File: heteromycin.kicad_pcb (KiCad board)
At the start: 4 copper layers, 200 x 100 mm, 379 parts, among them J1 M20-7832046, J10 DM3D-SF, J11 20021121-00010C4LF, J12 70543-0001, J13 70543-0001, J14 70543-0001, J15 70543-0001, J16 70543-0001, J17 70543-0001, J18 70543-0001, J19 70543-0001, J2 4DB-P108-06, J20 70543-0003, J21 70543-0002, J22 70543-0002, J23 70543-0002, J24 Conn_02x20_Odd_Even, J3 39531-1002, J4 39531-1002, J5 70543-0003, J6 70543-0003, J7 70543-0003, J8 70543-0003, J9 70543-0003, Q1 DMMT5401, Q10 PMPB11EN, Q11 PMPB11EN, Q12 PSMN1R2-30YLC,115, Q13 PSMN1R2-30YLC,115, Q14 PSMN1R2-30YLC,115, Q15 PMPB11EN, Q16 PMPB11EN, Q17 PMPB11EN, Q18 PMPB11EN, Q19 PMPB11EN, Q2 DMG2305UX, Q20 PMPB11EN, Q21 PMPB11EN, Q22 PMPB11EN, Q23 PMPB11EN, Q24 PMPB11EN, Q25 PMPB11EN, Q26 PMPB11EN, Q27 PMPB11EN, Q28 PMPB11EN, Q29 PMPB11EN, Q3 MMBT3904-7-F, Q30 PMPB11EN, Q31 PMPB11EN, Q32 PMPB11EN, Q33 PMPB11EN, Q34 PMPB11EN, Q35 PMPB11EN, Q36 PMPB11EN, Q37 PMPB11EN, Q38 PMPB11EN, Q39 PMPB11EN, Q4 PMPB11EN, Q40 PMPB11EN, Q41 PMPB11EN, Q42 PMPB11EN, Q43 PMPB11EN, Q44 PMPB11EN, Q45 PMPB11EN, Q46 PMPB11EN, Q47 PMPB11EN, Q48 PMPB11EN, Q49 PMPB11EN, Q5 PMPB11EN, Q50 PMPB11EN, Q6 PMPB11EN, Q7 PMPB11EN, Q8 PMPB11EN, Q9 PMPB11EN, SW1 PTS645VL39-2, U1 CAT24C32, U10 TMC2160-TA, U2 i3A, U3 AP7365-33WG-7, U4 CAT24C32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

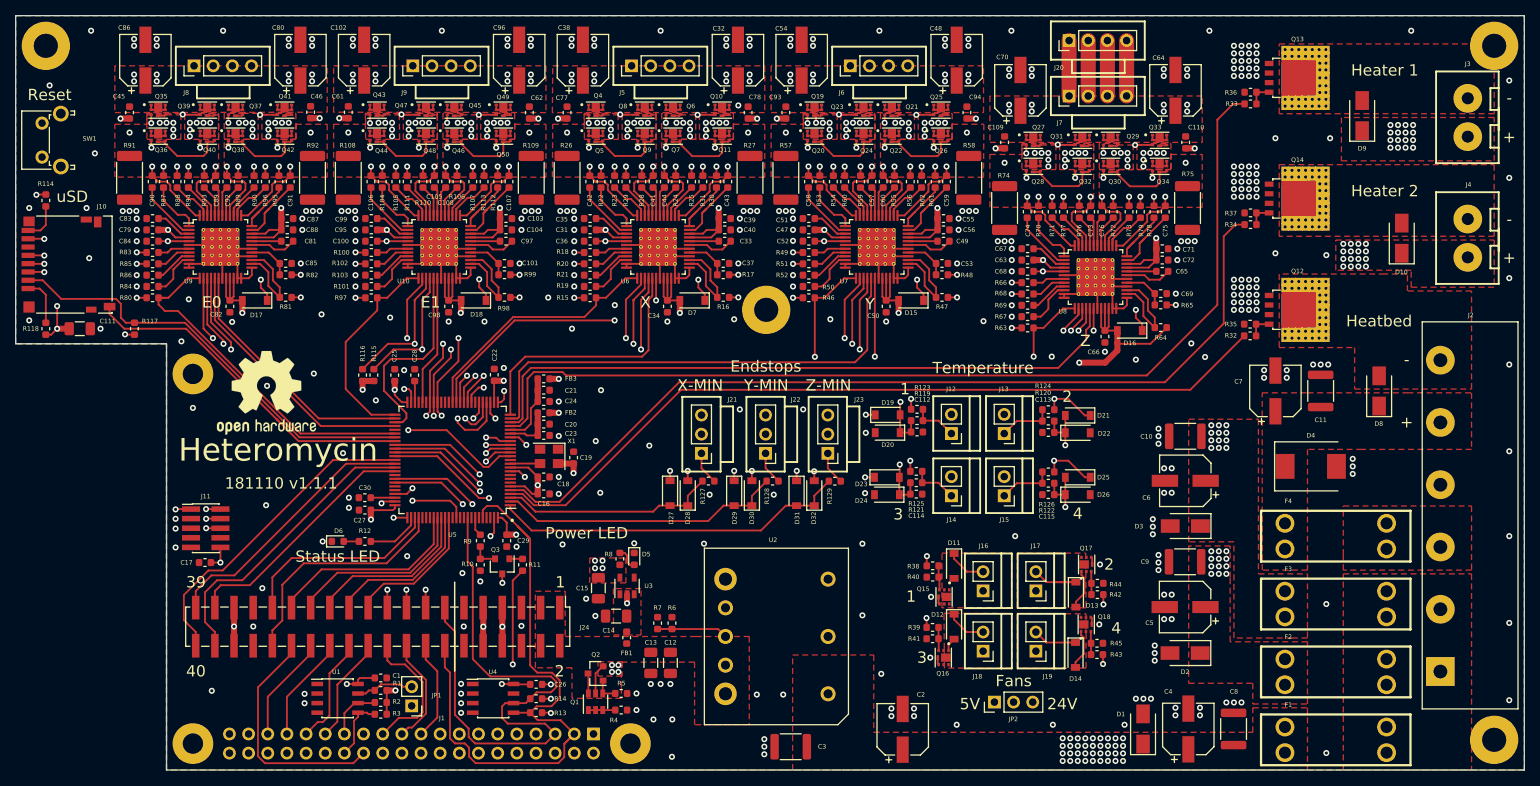
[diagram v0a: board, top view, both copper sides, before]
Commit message: Updated board to version 1.2
 * Switched small MOSFETs to SOT-23 package
 * Redesigned TMC*160 driver layout
 * Changed 01x03 to 02x03 jumper for FAN voltage selection
 * Switches STATUS_LED pin
 * Some copper pour optimizations
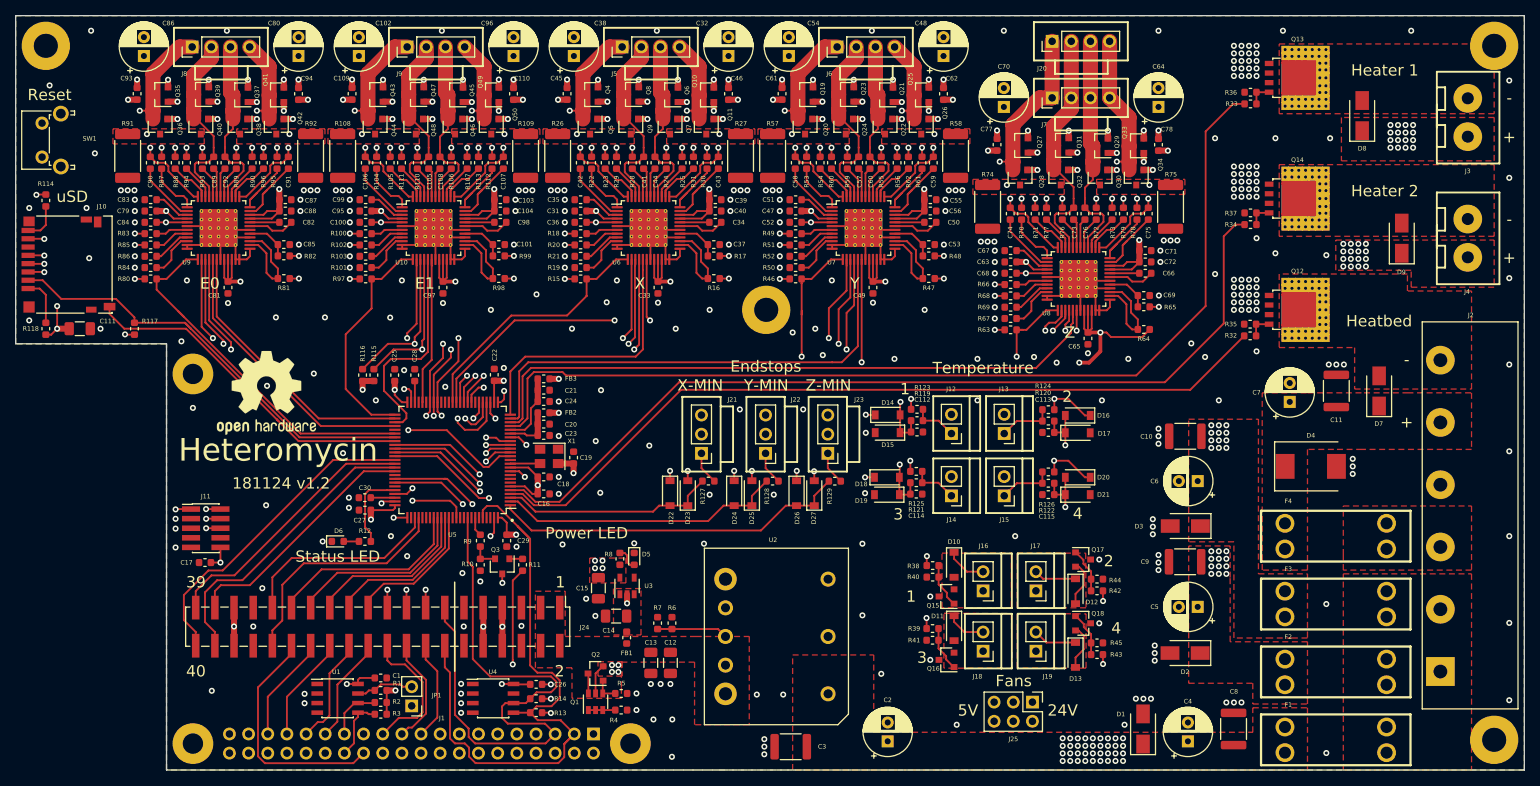
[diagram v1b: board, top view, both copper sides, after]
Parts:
- removed the D12 at (169.4, 131.0)
- removed the D15 at (163.7, 87.8)
- removed the D16 at (192.7, 91.8)
- removed the D17 at (76.7, 87.8)
- removed the D18 at (105.7, 87.8)
- removed the D7 at (134.7, 87.8)
- removed JP2: Jumper_3_Bridged12, Connector_PinHeader_2.54mm:PinHeader_1x03_P2.54mm_Vertical
- added D11: BAT54GWJ, Diode_SMD:D_SOD-123, F.Cu at (169.4, 131.2)
- added J25: Conn_02x03_Counter_Clockwise, Connector_PinHeader_2.54mm:PinHeader_2x03_P2.54mm_Vertical, F.Cu at (179.8, 141.0)
- C102, C2, C32, C38, C4, C48, C5, C54, C6, C64, C7, C70, C80, C86, C96: footprint Capacitor_SMD:CP_Elec_6.3x5.7 -> Capacitor_THT:CP_Radial_D6.3mm_P2.50mm
- C65: value 22nF -> 100nF
- C66: value 100nF -> 22nF
- Q10, Q11, Q15, Q16, Q17, Q18, Q19, Q20, Q21, Q22, Q23, Q24, Q25, Q26, Q27, Q28, Q29, Q30, Q31, Q32, Q33, Q34, Q35, Q36, Q37, Q38, Q39, Q4, Q40, Q41, Q42, Q43, Q44, Q45, Q46, Q47, Q48, Q49, Q5, Q50, Q6, Q7, Q8, Q9: value PMPB11EN -> IRLML0030TRPbF; footprint heteromycin:SOT1220 -> Package_TO_SOT_SMD:SOT-23
- moved C110 89.3 mm to (111.0, 60.4)
- moved C94 88.6 mm to (82.5, 60.4)
- moved C109 86.7 mm to (89.6, 60.4)
- moved C93 86.0 mm to (61.1, 60.4)
- moved C45 58.1 mm to (118.1, 60.4)
- moved C61 57.6 mm to (146.6, 60.4)
- moved C77 57.2 mm to (175.1, 67.1)
- moved C46 55.5 mm to (139.5, 60.4)
- moved C62 55.0 mm to (168.0, 60.4)
- moved C78 54.6 mm to (196.5, 67.1)
- moved C65 13.3 mm to (187.2, 92.8), turned to 270 degrees
- moved C66 9.95 mm to (194.8, 84.2), turned to 180 degrees
- moved Q34 3.58 mm to (193.6, 71.5), turned to 270 degrees
- moved R57 3.39 mm to (145.3, 68.6)
- moved R58 3.39 mm to (169.6, 68.6)
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- renumbered C34 to C33, C33 to C34, C50 to C49, C49 to C50, C82 to C81, C81 to C82, C98 to C97, C97 to C98, D11 to D10, D13 to D12, D14 to D13, D19 to D14, D20 to D15, D21 to D16, D22 to D17, D23 to D18, D24 to D19, D25 to D20, D26 to D21, D27 to D22, D28 to D23, D29 to D24, D30 to D25, D31 to D26, D32 to D27, D8 to D7, D9 to D8, D10 to D9
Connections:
- C65 pad 1: /Stepper Motor Z/CPO -> VDD3V3
- C65 pad 2: /Stepper Motor Z/CPI -> GND
- C66 pad 1: VDD3V3 -> /Stepper Motor Z/CPO
- C66 pad 2: GND -> /Stepper Motor Z/CPI
- J3 pad 1: VDD_HEAT1 -> HEAT1_OUT
- J3 pad 2: HEAT1_OUT -> VDD_HEAT1
- J4 pad 1: VDD_HEAT2 -> HEAT2_OUT
- J4 pad 2: HEAT2_OUT -> VDD_HEAT2
- Q10 pad 1: VDD24V -> Net-(Q10-Pad1)
- Q10 pad 3: Net-(Q10-Pad3) -> /Stepper Motor X/BMA2
- Q11 pad 1: /Stepper Motor X/BMA2 -> Net-(Q11-Pad1)
- Q15 pad 1: FAN1_OUT -> Net-(Q15-Pad1)
- Q15 pad 3: Net-(Q15-Pad3) -> GND
- Q16 pad 1: FAN3_OUT -> Net-(Q16-Pad1)
- Q16 pad 3: Net-(Q16-Pad3) -> GND
- Q17 pad 1: FAN2_OUT -> Net-(Q17-Pad1)
- Q17 pad 3: Net-(Q17-Pad3) -> GND
- Q18 pad 1: FAN4_OUT -> Net-(Q18-Pad1)
- Q18 pad 3: Net-(Q18-Pad3) -> GND
- Q19 pad 1: VDD24V -> Net-(Q19-Pad1)
- Q19 pad 3: Net-(Q19-Pad3) -> /Steper Motor Y/BMB1
- Q20 pad 1: /Steper Motor Y/BMB1 -> Net-(Q20-Pad1)
- Q21 pad 1: VDD24V -> Net-(Q21-Pad1)
- Q21 pad 3: Net-(Q21-Pad3) -> /Steper Motor Y/BMA1
- Q22 pad 1: /Steper Motor Y/BMA1 -> Net-(Q22-Pad1)
- Q23 pad 1: VDD24V -> Net-(Q23-Pad1)
- Q23 pad 3: Net-(Q23-Pad3) -> /Steper Motor Y/BMB2
- Q24 pad 1: /Steper Motor Y/BMB2 -> Net-(Q24-Pad1)
- Q24 pad 3: Net-(Q24-Pad3) -> Net-(Q20-Pad3)
- Q25 pad 1: VDD24V -> Net-(Q25-Pad1)
- Q25 pad 3: Net-(Q25-Pad3) -> /Steper Motor Y/BMA2
- Q26 pad 1: /Steper Motor Y/BMA2 -> Net-(Q26-Pad1)
- Q26 pad 3: Net-(Q26-Pad3) -> Net-(Q22-Pad3)
- Q27 pad 1: VDD24V -> Net-(Q27-Pad1)
- Q27 pad 3: Net-(Q27-Pad3) -> /Stepper Motor Z/BMB1
- Q28 pad 1: /Stepper Motor Z/BMB1 -> Net-(Q28-Pad1)
- Q29 pad 1: VDD24V -> Net-(Q29-Pad1)
- Q29 pad 3: Net-(Q29-Pad3) -> /Stepper Motor Z/BMA1
- Q30 pad 1: /Stepper Motor Z/BMA1 -> Net-(Q30-Pad1)
- Q31 pad 1: VDD24V -> Net-(Q31-Pad1)
- Q31 pad 3: Net-(Q31-Pad3) -> /Stepper Motor Z/BMB2
- Q32 pad 1: /Stepper Motor Z/BMB2 -> Net-(Q32-Pad1)
- Q32 pad 3: Net-(Q32-Pad3) -> Net-(Q28-Pad3)
- Q33 pad 1: VDD24V -> Net-(Q33-Pad1)
- Q33 pad 3: Net-(Q33-Pad3) -> /Stepper Motor Z/BMA2
- Q34 pad 1: /Stepper Motor Z/BMA2 -> Net-(Q34-Pad1)
- Q34 pad 3: Net-(Q34-Pad3) -> Net-(Q30-Pad3)
- Q35 pad 1: VDD24V -> Net-(Q35-Pad1)
- Q35 pad 3: Net-(Q35-Pad3) -> /Stepper Motor E0/BMB1
- Q36 pad 1: /Stepper Motor E0/BMB1 -> Net-(Q36-Pad1)
- Q37 pad 1: VDD24V -> Net-(Q37-Pad1)
- Q37 pad 3: Net-(Q37-Pad3) -> /Stepper Motor E0/BMA1
- Q38 pad 1: /Stepper Motor E0/BMA1 -> Net-(Q38-Pad1)
- Q39 pad 1: VDD24V -> Net-(Q39-Pad1)
- Q39 pad 3: Net-(Q39-Pad3) -> /Stepper Motor E0/BMB2
- Q4 pad 1: VDD24V -> Net-(Q4-Pad1)
- Q4 pad 3: Net-(Q4-Pad3) -> /Stepper Motor X/BMB1
- Q40 pad 1: /Stepper Motor E0/BMB2 -> Net-(Q40-Pad1)
- Q40 pad 3: Net-(Q40-Pad3) -> Net-(Q36-Pad3)
- Q41 pad 1: VDD24V -> Net-(Q41-Pad1)
- Q41 pad 3: Net-(Q41-Pad3) -> /Stepper Motor E0/BMA2
- Q42 pad 1: /Stepper Motor E0/BMA2 -> Net-(Q42-Pad1)
- Q42 pad 3: Net-(Q42-Pad3) -> Net-(Q38-Pad3)
- Q43 pad 1: VDD24V -> Net-(Q43-Pad1)
- Q43 pad 3: Net-(Q43-Pad3) -> /Stepper Motor E1/BMB1
- Q44 pad 1: /Stepper Motor E1/BMB1 -> Net-(Q44-Pad1)
- Q45 pad 1: VDD24V -> Net-(Q45-Pad1)
- Q45 pad 3: Net-(Q45-Pad3) -> /Stepper Motor E1/BMA1
- Q46 pad 1: /Stepper Motor E1/BMA1 -> Net-(Q46-Pad1)
- Q47 pad 1: VDD24V -> Net-(Q47-Pad1)
- Q47 pad 3: Net-(Q47-Pad3) -> /Stepper Motor E1/BMB2
- Q48 pad 1: /Stepper Motor E1/BMB2 -> Net-(Q48-Pad1)
- Q48 pad 3: Net-(Q48-Pad3) -> Net-(Q44-Pad3)
- Q49 pad 1: VDD24V -> Net-(Q49-Pad1)
- Q49 pad 3: Net-(Q49-Pad3) -> /Stepper Motor E1/BMA2
- Q5 pad 1: /Stepper Motor X/BMB1 -> Net-(Q5-Pad1)
- Q50 pad 1: /Stepper Motor E1/BMA2 -> Net-(Q50-Pad1)
- Q50 pad 3: Net-(Q50-Pad3) -> Net-(Q46-Pad3)
- Q6 pad 1: VDD24V -> Net-(Q6-Pad1)
- Q6 pad 3: Net-(Q6-Pad3) -> /Stepper Motor X/BMA1
- Q7 pad 1: /Stepper Motor X/BMA1 -> Net-(Q7-Pad1)
- Q7 pad 3: Net-(Q7-Pad3) -> Net-(Q11-Pad3)
- Q8 pad 1: VDD24V -> Net-(Q8-Pad1)
- Q8 pad 3: Net-(Q8-Pad3) -> /Stepper Motor X/BMB2
- Q9 pad 1: /Stepper Motor X/BMB2 -> Net-(Q9-Pad1)
- Q9 pad 3: Net-(Q9-Pad3) -> Net-(Q5-Pad3)
- R100 pad 1: Net-(Q44-Pad4) -> Net-(Q44-Pad3)
- R102 pad 2: Net-(Q46-Pad4) -> Net-(Q46-Pad3)
- R104 pad 2: Net-(Q43-Pad3) -> Net-(Q43-Pad1)
- R105 pad 2: Net-(Q44-Pad3) -> Net-(Q44-Pad1)
- R106 pad 2: Net-(Q45-Pad3) -> Net-(Q45-Pad1)
- R107 pad 2: Net-(Q46-Pad3) -> Net-(Q46-Pad1)
- R108 pad 2: Net-(Q44-Pad4) -> Net-(Q44-Pad3)
- R109 pad 2: Net-(Q46-Pad4) -> Net-(Q46-Pad3)
- R110 pad 1: Net-(Q47-Pad3) -> Net-(Q47-Pad1)
- R111 pad 1: Net-(Q48-Pad3) -> Net-(Q48-Pad1)
- R112 pad 1: Net-(Q49-Pad3) -> Net-(Q49-Pad1)
- R113 pad 1: Net-(Q50-Pad3) -> Net-(Q50-Pad1)
- R18 pad 1: Net-(Q5-Pad4) -> Net-(Q5-Pad3)
- R20 pad 2: Net-(Q11-Pad4) -> Net-(Q11-Pad3)
- R22 pad 2: Net-(Q4-Pad3) -> Net-(Q4-Pad1)
- R23 pad 2: Net-(Q5-Pad3) -> Net-(Q5-Pad1)
- R24 pad 2: Net-(Q6-Pad3) -> Net-(Q6-Pad1)
- R25 pad 2: Net-(Q7-Pad3) -> Net-(Q7-Pad1)
- R26 pad 2: Net-(Q5-Pad4) -> Net-(Q5-Pad3)
- R27 pad 2: Net-(Q11-Pad4) -> Net-(Q11-Pad3)
- R28 pad 1: Net-(Q8-Pad3) -> Net-(Q8-Pad1)
- R29 pad 1: Net-(Q9-Pad3) -> Net-(Q9-Pad1)
- R30 pad 1: Net-(Q10-Pad3) -> Net-(Q10-Pad1)
- R31 pad 1: Net-(Q11-Pad3) -> Net-(Q11-Pad1)
- R38 pad 1: Net-(Q15-Pad3) -> Net-(Q15-Pad1)
- R39 pad 1: Net-(Q16-Pad3) -> Net-(Q16-Pad1)
- R40 pad 2: Net-(Q15-Pad3) -> Net-(Q15-Pad1)
- R41 pad 2: Net-(Q16-Pad3) -> Net-(Q16-Pad1)
- R42 pad 1: Net-(Q17-Pad3) -> Net-(Q17-Pad1)
- R43 pad 1: Net-(Q18-Pad3) -> Net-(Q18-Pad1)
- R44 pad 2: Net-(Q17-Pad3) -> Net-(Q17-Pad1)
- R45 pad 2: Net-(Q18-Pad3) -> Net-(Q18-Pad1)
- R49 pad 1: Net-(Q20-Pad4) -> Net-(Q20-Pad3)
- R51 pad 2: Net-(Q22-Pad4) -> Net-(Q22-Pad3)
- R53 pad 2: Net-(Q19-Pad3) -> Net-(Q19-Pad1)
- R54 pad 2: Net-(Q20-Pad3) -> Net-(Q20-Pad1)
- R55 pad 2: Net-(Q21-Pad3) -> Net-(Q21-Pad1)
- R56 pad 2: Net-(Q22-Pad3) -> Net-(Q22-Pad1)
- R57 pad 2: Net-(Q20-Pad4) -> Net-(Q20-Pad3)
- R58 pad 2: Net-(Q22-Pad4) -> Net-(Q22-Pad3)
- R59 pad 1: Net-(Q23-Pad3) -> Net-(Q23-Pad1)
- R60 pad 1: Net-(Q24-Pad3) -> Net-(Q24-Pad1)
- R61 pad 1: Net-(Q25-Pad3) -> Net-(Q25-Pad1)
- R62 pad 1: Net-(Q26-Pad3) -> Net-(Q26-Pad1)
- R66 pad 1: Net-(Q28-Pad4) -> Net-(Q28-Pad3)
- R68 pad 2: Net-(Q30-Pad4) -> Net-(Q30-Pad3)
- R70 pad 2: Net-(Q27-Pad3) -> Net-(Q27-Pad1)
- R71 pad 2: Net-(Q28-Pad3) -> Net-(Q28-Pad1)
- R72 pad 2: Net-(Q29-Pad3) -> Net-(Q29-Pad1)
- R73 pad 2: Net-(Q30-Pad3) -> Net-(Q30-Pad1)
- R74 pad 2: Net-(Q28-Pad4) -> Net-(Q28-Pad3)
- R75 pad 2: Net-(Q30-Pad4) -> Net-(Q30-Pad3)
- R76 pad 1: Net-(Q31-Pad3) -> Net-(Q31-Pad1)
- R77 pad 1: Net-(Q32-Pad3) -> Net-(Q32-Pad1)
- R78 pad 1: Net-(Q33-Pad3) -> Net-(Q33-Pad1)
- R79 pad 1: Net-(Q34-Pad3) -> Net-(Q34-Pad1)
- R83 pad 1: Net-(Q36-Pad4) -> Net-(Q36-Pad3)
- R85 pad 2: Net-(Q38-Pad4) -> Net-(Q38-Pad3)
- R87 pad 2: Net-(Q35-Pad3) -> Net-(Q35-Pad1)
- R88 pad 2: Net-(Q36-Pad3) -> Net-(Q36-Pad1)
- R89 pad 2: Net-(Q37-Pad3) -> Net-(Q37-Pad1)
- R90 pad 2: Net-(Q38-Pad3) -> Net-(Q38-Pad1)
- R91 pad 2: Net-(Q36-Pad4) -> Net-(Q36-Pad3)
- R92 pad 2: Net-(Q38-Pad4) -> Net-(Q38-Pad3)
- R93 pad 1: Net-(Q39-Pad3) -> Net-(Q39-Pad1)
- R94 pad 1: Net-(Q40-Pad3) -> Net-(Q40-Pad1)
- R95 pad 1: Net-(Q41-Pad3) -> Net-(Q41-Pad1)
- R96 pad 1: Net-(Q42-Pad3) -> Net-(Q42-Pad1)
- U5 pad 71: Net-(U5-Pad71) -> /MCU/STATUS_LED
- U5 pad 77: /MCU/STATUS_LED -> Net-(U5-Pad77)
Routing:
- net VDD24V: track 162.7 -> 110.5 mm, vias 92 -> 76
- net Net-(Q28-Pad4): track 47.2 -> 0.00 mm, vias 2 -> 0
- net Net-(Q20-Pad4): track 47.2 -> 0.00 mm, vias 2 -> 0
- net Net-(Q5-Pad4): track 47.2 -> 0.00 mm, vias 2 -> 0
- net Net-(Q44-Pad4): track 47.2 -> 0.00 mm, vias 2 -> 0
- net Net-(Q36-Pad4): track 47.2 -> 0.00 mm, vias 2 -> 0
- net Net-(Q11-Pad4): track 44.4 -> 0.00 mm, vias 2 -> 0
- net Net-(Q30-Pad4): track 44.4 -> 0.00 mm, vias 2 -> 0
- net Net-(Q22-Pad4): track 44.4 -> 0.00 mm, vias 2 -> 0
- net Net-(Q46-Pad4): track 44.4 -> 0.00 mm, vias 2 -> 0
- net Net-(Q38-Pad4): track 44.4 -> 0.00 mm, vias 2 -> 0
- net Net-(Q11-Pad3): track 5.30 -> 31.6 mm
- net Net-(Q36-Pad3): track 6.58 -> 31.7 mm
- net Net-(Q5-Pad3): track 6.58 -> 31.7 mm
- net Net-(Q44-Pad3): track 6.58 -> 31.7 mm
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- added copper zone on F.Cu, net Net-(Q11-Pad3)
- added copper zone on F.Cu, net Net-(Q20-Pad3)
- added copper zone on F.Cu, net Net-(Q22-Pad3)
- added copper zone on F.Cu, net Net-(Q28-Pad3)
- added copper zone on F.Cu, net Net-(Q30-Pad3)
- added copper zone on F.Cu, net Net-(Q36-Pad3)
- added copper zone on F.Cu, net Net-(Q38-Pad3)
- added copper zone on F.Cu, net Net-(Q44-Pad3)
- added copper zone on F.Cu, net Net-(Q46-Pad3)
- added copper zone on F.Cu, net Net-(Q5-Pad3)
- removed copper zone on F.Cu, net /Steper Motor Y/BMA1
- removed copper zone on In2.Cu, net /Steper Motor Y/BMA1
- removed copper zone on F.Cu, net /Steper Motor Y/BMA2
- removed copper zone on In2.Cu, net /Steper Motor Y/BMA2
- removed copper zone on F.Cu, net /Steper Motor Y/BMB1
- removed copper zone on In2.Cu, net /Steper Motor Y/BMB1
- removed copper zone on F.Cu, net /Steper Motor Y/BMB2
- removed copper zone on In2.Cu, net /Steper Motor Y/BMB2
- removed copper zone on F.Cu, net /Stepper Motor E0/BMA1
- removed copper zone on In2.Cu, net /Stepper Motor E0/BMA1
- removed copper zone on F.Cu, net /Stepper Motor E0/BMA2
- removed copper zone on In2.Cu, net /Stepper Motor E0/BMA2
- removed copper zone on F.Cu, net /Stepper Motor E0/BMB1
- removed copper zone on In2.Cu, net /Stepper Motor E0/BMB1
- removed copper zone on F.Cu, net /Stepper Motor E0/BMB2
- removed copper zone on In2.Cu, net /Stepper Motor E0/BMB2
- removed copper zone on F.Cu, net /Stepper Motor E1/BMA1
- removed copper zone on In2.Cu, net /Stepper Motor E1/BMA1
- removed copper zone on F.Cu, net /Stepper Motor E1/BMA2
- removed copper zone on In2.Cu, net /Stepper Motor E1/BMA2
- removed copper zone on F.Cu, net /Stepper Motor E1/BMB1
- removed copper zone on In2.Cu, net /Stepper Motor E1/BMB1
- removed copper zone on F.Cu, net /Stepper Motor E1/BMB2
- removed copper zone on In2.Cu, net /Stepper Motor E1/BMB2
- removed copper zone on F.Cu, net /Stepper Motor X/BMA1
- removed copper zone on In2.Cu, net /Stepper Motor X/BMA1
- removed copper zone on F.Cu, net /Stepper Motor X/BMA2
- removed copper zone on In2.Cu, net /Stepper Motor X/BMA2
- removed copper zone on F.Cu, net /Stepper Motor X/BMB1
- removed copper zone on In2.Cu, net /Stepper Motor X/BMB1
- removed copper zone on F.Cu, net /Stepper Motor X/BMB2
- removed copper zone on In2.Cu, net /Stepper Motor X/BMB2
- removed copper zone on F.Cu, net /Stepper Motor Z/BMA1
- removed copper zone on In2.Cu, net /Stepper Motor Z/BMA1
- removed copper zone on F.Cu, net /Stepper Motor Z/BMA2
- removed copper zone on In2.Cu, net /Stepper Motor Z/BMA2
- removed copper zone on F.Cu, net /Stepper Motor Z/BMB1
- removed copper zone on In2.Cu, net /Stepper Motor Z/BMB1
- removed copper zone on F.Cu, net /Stepper Motor Z/BMB2
- removed copper zone on In2.Cu, net /Stepper Motor Z/BMB2
- removed copper zone on F.Cu, net Net-(Q11-Pad4)
- removed copper zone on F.Cu, net Net-(Q20-Pad4)
- removed copper zone on F.Cu, net Net-(Q22-Pad4)
- removed copper zone on F.Cu, net Net-(Q28-Pad4)
- removed copper zone on F.Cu, net Net-(Q30-Pad4)
- removed copper zone on F.Cu, net Net-(Q36-Pad4)
- removed copper zone on F.Cu, net Net-(Q38-Pad4)
- removed copper zone on F.Cu, net Net-(Q44-Pad4)
- removed copper zone on F.Cu, net Net-(Q46-Pad4)
- removed copper zone on F.Cu, net Net-(Q5-Pad4)
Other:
- board text added: "181124 v1.2"
- board text removed: "181110 v1.1.1"

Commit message: Increased sense resistor value to 0.1
This will result in a maximum 2.3A current for the stepper.
This should act as a more sensible default. Of course the user
can replace the sense resistors as they see fit. As long as they
they don't stress the termal budget of the driver MOSFET that is.
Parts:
- R108, R109, R26, R27, R57, R58, R74, R75, R91, R92: value 0.075 -> 0.1
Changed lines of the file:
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@@
       (effects (font (size 0.6 0.6) (thickness 0.1)))
     )
-    (fp_text value 0.075 (at 0 2.62 90) (layer F.Fab)
+    (fp_text value 0.1 (at 0 2.62 90) (layer F.Fab)
       (effects (font (size 0.6 0.6) (thickness 0.1)))
     )
@@
       (effects (font (size 0.6 0.6) (thickness 0.1)))
     )
-    (fp_text value 0.075 (at 0 2.62 90) (layer F.Fab)
+    (fp_text value 0.1 (at 0 2.62 90) (layer F.Fab)
       (effects (font (size 0.6 0.6) (thickness 0.1)))
     )
@@
       (effects (font (size 0.6 0.6) (thickness 0.1)))
     )
-    (fp_text value 0.075 (at 0 2.62 90) (layer F.Fab)
+    (fp_text value 0.1 (at 0 2.62 90) (layer F.Fab)
       (effects (font (size 0.6 0.6) (thickness 0.1)))
     )
@@
       (effects (font (size 0.6 0.6) (thickness 0.1)))
     )
-    (fp_text value 0.075 (at 0 2.62 90) (layer F.Fab)
+    (fp_text value 0.1 (at 0 2.62 90) (layer F.Fab)
       (effects (font (size 0.6 0.6) (thickness 0.1)))
     )
@@
       (effects (font (size 0.6 0.6) (thickness 0.1)))
     )
-    (fp_text value 0.075 (at 0 2.62 90) (layer F.Fab)
+    (fp_text value 0.1 (at 0 2.62 90) (layer F.Fab)
       (effects (font (size 0.6 0.6) (thickness 0.1)))
     )
@@
       (effects (font (size 0.6 0.6) (thickness 0.1)))
     )
-    (fp_text value 0.075 (at 0 2.62 90) (layer F.Fab)
+    (fp_text value 0.1 (at 0 2.62 90) (layer F.Fab)
       (effects (font (size 0.6 0.6) (thickness 0.1)))
     )
@@
       (effects (font (size 0.6 0.6) (thickness 0.1)))
     )
-    (fp_text value 0.075 (at 0 2.62 90) (layer F.Fab)
+    (fp_text value 0.1 (at 0 2.62 90) (layer F.Fab)
       (effects (font (size 0.6 0.6) (thickness 0.1)))
     )
@@
       (effects (font (size 0.6 0.6) (thickness 0.1)))
     )
-    (fp_text value 0.075 (at 0 2.62 90) (layer F.Fab)
+    (fp_text value 0.1 (at 0 2.62 90) (layer F.Fab)
       (effects (font (size 0.6 0.6) (thickness 0.1)))
     )
@@
       (effects (font (size 0.6 0.6) (thickness 0.1)))
     )
-    (fp_text value 0.075 (at 0 2.62 90) (layer F.Fab)
+    (fp_text value 0.1 (at 0 2.62 90) (layer F.Fab)
       (effects (font (size 0.6 0.6) (thickness 0.1)))
     )
@@
       (effects (font (size 0.6 0.6) (thickness 0.1)))
     )
-    (fp_text value 0.075 (at 0 2.62 90) (layer F.Fab)
+    (fp_text value 0.1 (at 0 2.62 90) (layer F.Fab)
       (effects (font (size 0.6 0.6) (thickness 0.1)))
     )
@@
   (via (at 204 66.25) (size 0.8) (drill 0.4) (layers F.Cu B.Cu) (net 4))
   (via (at 94.75 119) (size 0.8) (drill 0.4) (layers F.Cu B.Cu) (net 4))
+  (via (at 180 95.25) (size 0.8) (drill 0.4) (layers F.Cu B.Cu) (net 4))
   (via (at 103.3 85.25) (size 0.8) (drill 0.4) (layers F.Cu B.Cu) (net 5))
   (segment (start 103.3 85.25) (end 101.65 85.25) (width 0.5) (layer F.Cu) (net 5))
@@
   (segment (start 186 96) (end 187.3 96) (width 0.5) (layer F.Cu) (net 5))
   (segment (start 187.3 96) (end 188.8 94.5) (width 0.5) (layer F.Cu) (net 5))
-  (via (at 180 95.25) (size 0.8) (drill 0.4) (layers F.Cu B.Cu) (net 4))
   (segment (start 194.875888 92.061612) (end 195.3375 91.6) (width 0.25) (layer F.Cu) (net 5))
   (segment (start 194.3375 92.6) (end 194.875888 92.061612) (width 0.25) (layer F.Cu) (net 5))

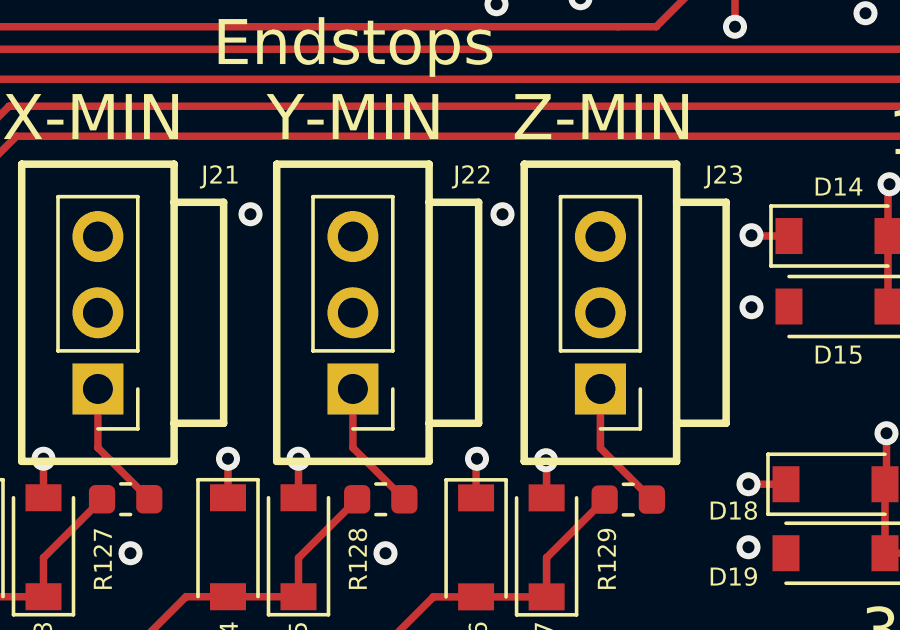
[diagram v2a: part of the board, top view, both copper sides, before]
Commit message: Add silkscreen explanation for endstop pins
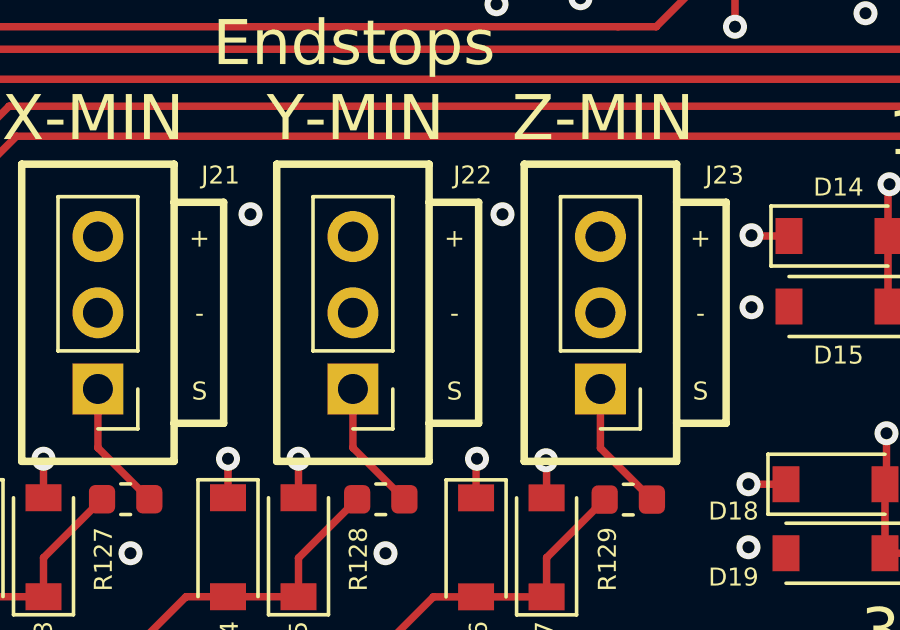
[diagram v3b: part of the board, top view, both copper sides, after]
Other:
- board text added: "S"
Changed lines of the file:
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@@
   (general
     (thickness 1.6)
-    (drawings 72)
+    (drawings 81)
     (tracks 3993)
     (zones 0)
@@
     )
   )
+  (gr_text S (at 156 108.1) (layer F.SilkS)
+    (effects (font (size 0.6 0.6) (thickness 0.1)))
+  )
+  (gr_text S (at 147.8 108.1) (layer F.SilkS)
+    (effects (font (size 0.6 0.6) (thickness 0.1)))
+  )
+  (gr_text S (at 139.3 108.1) (layer F.SilkS)
+    (effects (font (size 0.6 0.6) (thickness 0.1)))
+  )
+  (gr_text - (at 139.3 105.5) (layer F.SilkS)
+    (effects (font (size 0.6 0.6) (thickness 0.1)))
+  )
+  (gr_text - (at 147.8 105.5) (layer F.SilkS)
+    (effects (font (size 0.6 0.6) (thickness 0.1)))
+  )
+  (gr_text - (at 156 105.5) (layer F.SilkS)
+    (effects (font (size 0.6 0.6) (thickness 0.1)))
+  )
+  (gr_text + (at 156 103) (layer F.SilkS)
+    (effects (font (size 0.6 0.6) (thickness 0.1)))
+  )
+  (gr_text + (at 147.8 103) (layer F.SilkS)
+    (effects (font (size 0.6 0.6) (thickness 0.1)))
+  )
+  (gr_text + (at 139.3 103) (layer F.SilkS)
+    (effects (font (size 0.6 0.6) (thickness 0.1)))
+  )
   (gr_text E1 (at 99.25 85.5) (layer F.SilkS)

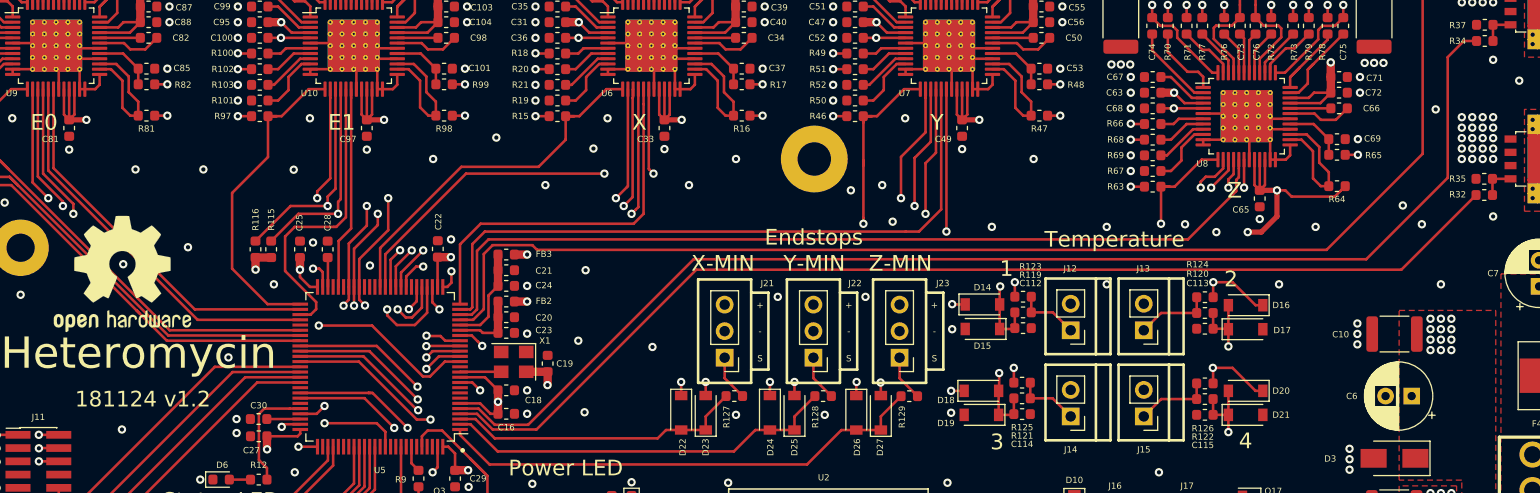
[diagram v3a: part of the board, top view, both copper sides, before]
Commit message: Connected TMC DIAG pins to MCU
We had some pins free, so I decided to connect them, so that we
don't need to use the ENDSTOP OVER SPI feature.
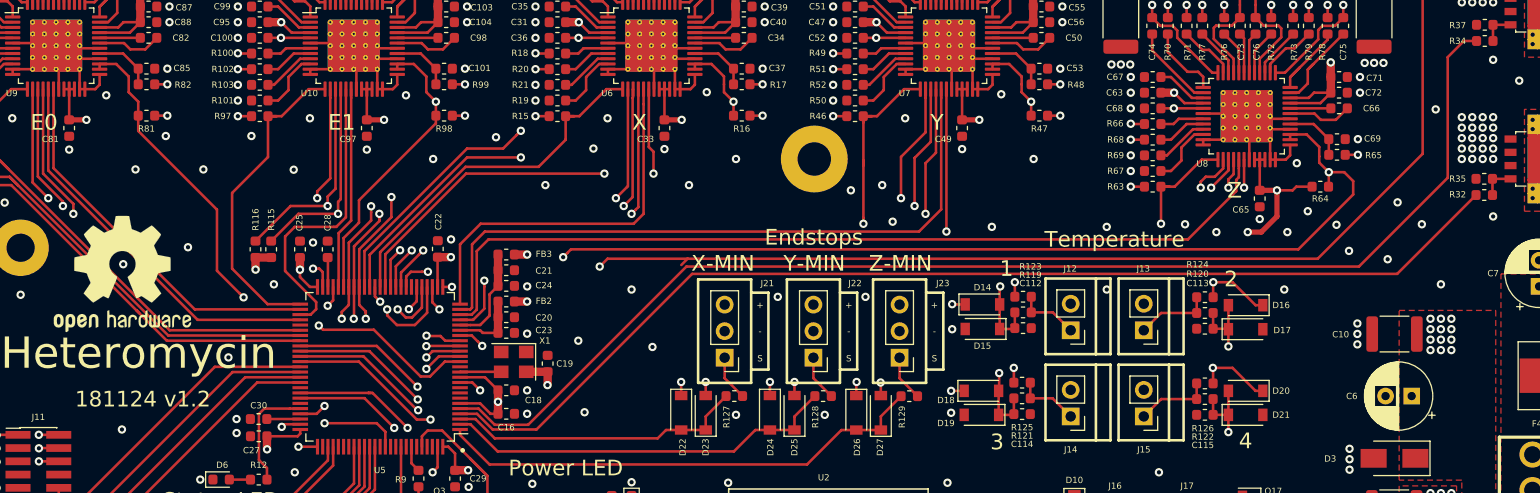
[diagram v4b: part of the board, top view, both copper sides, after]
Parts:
- moved R64 1.60 mm to (192.9, 91.7), turned to 180 degrees
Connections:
- U5 pad 39: Net-(U5-Pad39) -> /Stepper Motor Z/DIAG
- U5 pad 40: Net-(U5-Pad40) -> /Steper Motor Y/DIAG
- U5 pad 41: Net-(U5-Pad41) -> /Stepper Motor X/DIAG
- U5 pad 45: Net-(U5-Pad45) -> /Stepper Motor E1/DIAG
- U5 pad 47: Net-(U5-Pad47) -> /Stepper Motor E0/DIAG
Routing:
- net /Stepper Motor Z/DIAG: track 14.5 -> 111.2 mm, vias 0 -> 3
- net /Steper Motor Y/DIAG: track 14.5 -> 80.4 mm, vias 0 -> 2
- net /Stepper Motor X/DIAG: track 14.5 -> 52.6 mm, vias 0 -> 2
- net VDD3V3: track 191.0 -> 160.9 mm
- net /Stepper Motor E0/DIAG: track 14.5 -> 39.9 mm, vias 0 -> 2
- net /Stepper Motor E1/DIAG: track 14.4 -> 28.0 mm, vias 0 -> 1
- net GND: track 158.4 -> 157.2 mm, vias 315 -> 325
- net /MCU/PWM_HEAT1: track 132.1 -> 131.0 mm, vias 0 -> 2
- net /Stepper Motor Z/DIR: track 88.4 -> 87.7 mm
